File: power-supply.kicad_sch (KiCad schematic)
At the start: 9 parts, among them J1 KRE, J10 KRE, J12 Conn_01x04, J15 Conn_01x04, J3 KRE

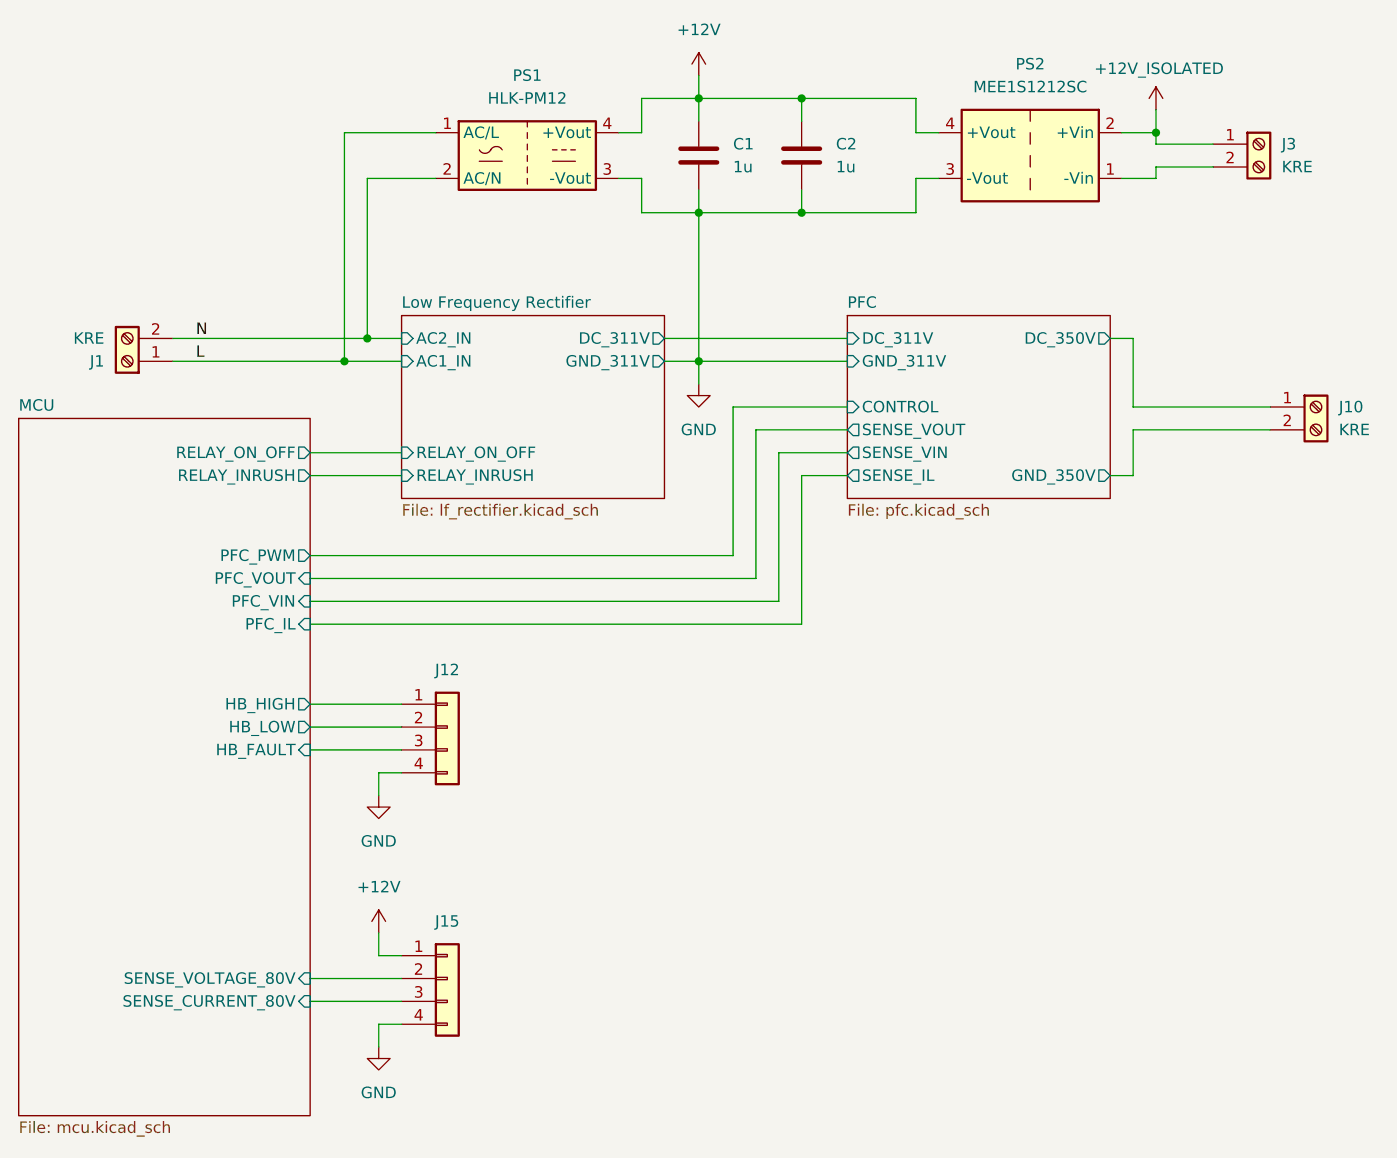
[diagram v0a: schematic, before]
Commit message: docs: add 3D renders, comprehensive README, CERN-OHL-S license, and update PCB routing
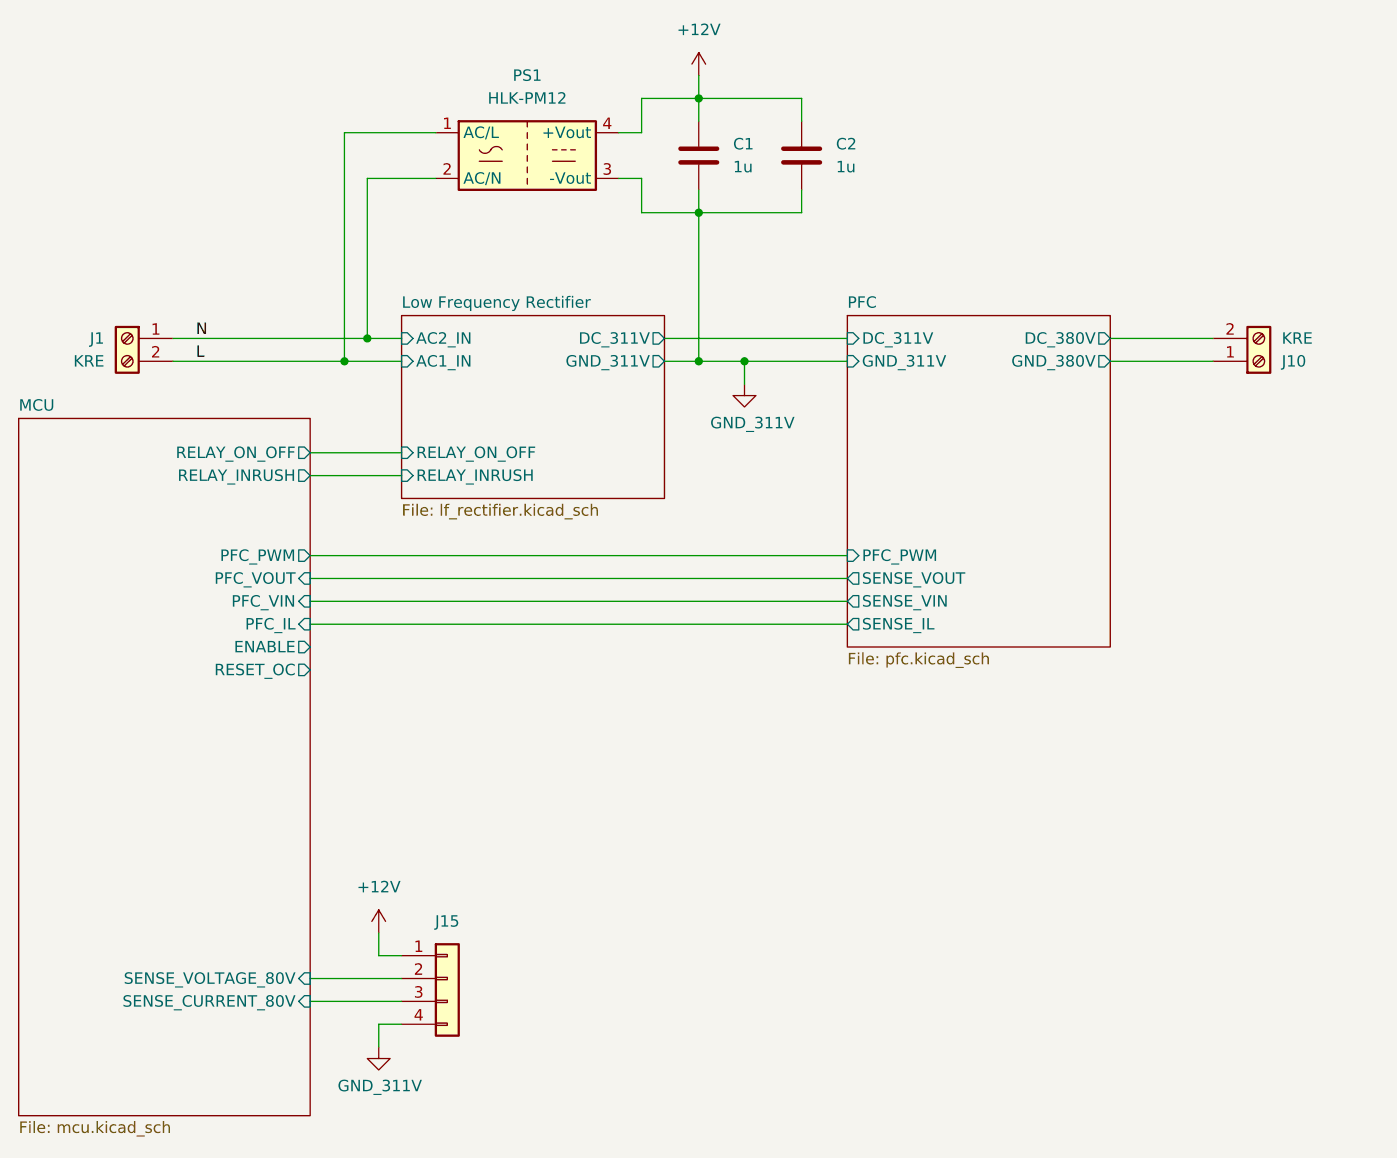
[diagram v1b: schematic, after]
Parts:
- removed J12: Conn_01x04, Connector_JST:JST_XH_B4B-XH-A_1x04_P2.50mm_Vertical, symbol Connector_Generic:Conn_01x04
- removed J3: KRE, TerminalBlock_Phoenix:TerminalBlock_Phoenix_MKDS-1,5-2-5.08_1x02_P5.08mm_Horizontal, symbol Connector:Screw_Terminal_01x02
- removed PS2: MEE1S1212SC, Converter_DCDC:Converter_DCDC_Murata_MEE1SxxxxSC_THT, symbol Converter_DCDC:MEE1S1212SC
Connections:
- net L: now also J1.2 (Pin_2); no longer J1.1 (Pin_1)
- net N: now also J1.1 (Pin_1); no longer J1.2 (Pin_2)
- net GND renamed GND_311V
- net PFC/DC_350V renamed PFC/GND_380V
- net PFC/GND_350V renamed PFC/DC_380V
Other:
- sheet MCU ports: added ENABLE, RESET_OC; removed HB_FAULT, HB_HIGH, HB_LOW
- sheet PFC ports: added DC_380V, GND_380V, PFC_PWM; removed CONTROL, DC_350V, GND_350V

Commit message: pcb: atualizar layout 2D da placa e esquematicos
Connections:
- net L: now also J1.1 (Pin_1); no longer J1.2 (Pin_2)
- net N: now also J1.2 (Pin_2); no longer J1.1 (Pin_1)
- net PFC/DC_380V: now also J10.1 (Pin_1); no longer J10.2 (Pin_2)
- net PFC/GND_380V: now also J10.2 (Pin_2); no longer J10.1 (Pin_1)
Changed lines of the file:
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@@
+	)
+	(symbol
+		(lib_id "Connector:Screw_Terminal_01x02")
+		(at 83.82 72.39 180)
+		(unit 1)
+		(body_style 1)
+		(exclude_from_sim no)
+		(in_bom yes)
+		(on_board yes)
+		(in_pos_files yes)
+		(dnp no)
+		(property "Reference" "J1"
+			(at 81.28 72.3901 0)
+			(show_name no)
+			(do_not_autoplace no)
+			(effects
+				(font
+					(size 1.27 1.27)
+				)
+				(justify left)
+			)
+		)
+		(property "Value" "KRE"
+			(at 81.28 69.8501 0)
+			(show_name no)
+			(do_not_autoplace no)
+			(effects
+				(font
+					(size 1.27 1.27)
+				)
+				(justify left)
+			)
+		)
+		(property "Footprint" "TerminalBlock_Phoenix:TerminalBlock_Phoenix_MKDS-1,5-2-5.08_1x02_P5.08mm_Horizontal"
+			(at 83.82 72.39 0)
+			(hide yes)
+			(show_name no)
+			(do_not_autoplace no)
+			(effects
+				(font
+					(size 1.27 1.27)
+				)
+			)
+		)
+		(property "Datasheet" ""
+			(at 83.82 72.39 0)
+			(hide yes)
+			(show_name no)
+			(do_not_autoplace no)
+			(effects
+				(font
+					(size 1.27 1.27)
+				)
+			)
+		)
+		(property "Description" "Generic screw terminal, single row, 01x02, script generated (kicad-library-utils/schlib/autogen/connector/)"
+			(at 83.82 72.39 0)
+			(hide yes)
+			(show_name no)
+			(do_not_autoplace no)
+			(effects
+				(font
+					(size 1.27 1.27)
+				)
+			)
+		)
+		(pin "1"
+		)
+		(pin "2"
+		)
+		(instances
+			(project "power-supply"
+				(path "/7202e823-25ba-4b77-8a88-a38eb2bf69b9"
+					(reference "J1")
+					(unit 1)
+				)
+			)
+		)
+	)
+	(symbol
+		(lib_id "Connector:Screw_Terminal_01x02")
+		(at 209.55 69.85 0)
+		(unit 1)
+		(body_style 1)
+		(exclude_from_sim no)
+		(in_bom yes)
+		(on_board yes)
+		(in_pos_files yes)
+		(dnp no)
+		(property "Reference" "J10"
+			(at 212.09 69.8499 0)
+			(show_name no)
+			(do_not_autoplace no)
+			(effects
+				(font
+					(size 1.27 1.27)
+				)
+				(justify left)
+			)
+		)
+		(property "Value" "KRE"
+			(at 212.09 72.3899 0)
+			(show_name no)
+			(do_not_autoplace no)
+			(effects
+				(font
+					(size 1.27 1.27)
+				)
+				(justify left)
+			)
+		)
+		(property "Footprint" "TerminalBlock_Phoenix:TerminalBlock_Phoenix_MKDS-1,5-2-5.08_1x02_P5.08mm_Horizontal"
+			(at 209.55 69.85 0)
+			(hide yes)
+			(show_name no)
+			(do_not_autoplace no)
+			(effects
+				(font
+					(size 1.27 1.27)
+				)
+			)
+		)
+		(property "Datasheet" ""
+			(at 209.55 69.85 0)
+			(hide yes)
+			(show_name no)
+			(do_not_autoplace no)
+			(effects
+				(font
+					(size 1.27 1.27)
+				)
+			)
+		)
+		(property "Description" "Generic screw terminal, single row, 01x02, script generated (kicad-library-utils/schlib/autogen/connector/)"
+			(at 209.55 69.85 0)
+			(hide yes)
+			(show_name no)
+			(do_not_autoplace no)
+			(effects
+				(font
+					(size 1.27 1.27)
+				)
+			)
+		)
+		(pin "1"
+		)
+		(pin "2"
+		)
+		(instances
+			(project "power-supply"
+				(path "/7202e823-25ba-4b77-8a88-a38eb2bf69b9"
+					(reference "J10")
+					(unit 1)
+				)
+			)
+		)
 	)
 	(symbol
@@
 	)
 	(symbol
-		(lib_id "Connector:Screw_Terminal_01x02")
-		(at 209.55 72.39 0)
-		(mirror x)
-		(unit 1)
-		(body_style 1)
-		(exclude_from_sim no)
-		(in_bom yes)
-		(on_board yes)
-		(in_pos_files yes)
-		(dnp no)
-		(property "Reference" "J10"
-			(at 212.09 72.3901 0)
-			(show_name no)
-			(do_not_autoplace no)
-			(effects
-				(font
-					(size 1.27 1.27)
-				)
-				(justify left)
-			)
-		)
-		(property "Value" "KRE"
-			(at 212.09 69.8501 0)
-			(show_name no)
-			(do_not_autoplace no)
-			(effects
-				(font
-					(size 1.27 1.27)
-				)
-				(justify left)
-			)
-		)
-		(property "Footprint" "TerminalBlock_Phoenix:TerminalBlock_Phoenix_MKDS-1,5-2-5.08_1x02_P5.08mm_Horizontal"
-			(at 209.55 72.39 0)
-			(hide yes)
-			(show_name no)
-			(do_not_autoplace no)
-			(effects
-				(font
-					(size 1.27 1.27)
-				)
-			)
-		)
-		(property "Datasheet" ""
-			(at 209.55 72.39 0)
-			(hide yes)
-			(show_name no)
-			(do_not_autoplace no)
-			(effects
-				(font
-					(size 1.27 1.27)
-				)
-			)
-		)
-		(property "Description" "Generic screw terminal, single row, 01x02, script generated (kicad-library-utils/schlib/autogen/connector/)"
-			(at 209.55 72.39 0)
-			(hide yes)
-			(show_name no)
-			(do_not_autoplace no)
-			(effects
-				(font
-					(size 1.27 1.27)
-				)
-			)
-		)
-		(pin "1"
-		)
-		(pin "2"
-		)
-		(instances
-			(project "power-supply"
-				(path "/7202e823-25ba-4b77-8a88-a38eb2bf69b9"
-					(reference "J10")
-					(unit 1)
-				)
-			)
-		)
-	)
-	(symbol
 		(lib_id "power:+12V")
 		(at 147.32 40.64 0)
@@
 					(unit 1)
 				)
-			)
-		)
-	)
-	(symbol
-		(lib_id "Connector:Screw_Terminal_01x02")
-		(at 83.82 69.85 0)
-		(mirror y)
-		(unit 1)
-		(body_style 1)
-		(exclude_from_sim no)
-		(in_bom yes)
-		(on_board yes)
-		(in_pos_files yes)
-		(dnp no)
-		(property "Reference" "J1"
-			(at 81.28 69.8499 0)
-			(show_name no)
-			(do_not_autoplace no)
-			(effects
-				(font
-					(size 1.27 1.27)
-				)
-				(justify left)
-			)
-		)
-		(property "Value" "KRE"
-			(at 81.28 72.3899 0)
-			(show_name no)
-			(do_not_autoplace no)
-			(effects
-				(font
-					(size 1.27 1.27)
-				)
-				(justify left)
-			)
-		)
-		(property "Footprint" "TerminalBlock_Phoenix:TerminalBlock_Phoenix_MKDS-1,5-2-5.08_1x02_P5.08mm_Horizontal"
-			(at 83.82 69.85 0)
-			(hide yes)
-			(show_name no)
-			(do_not_autoplace no)
-			(effects
-				(font
-					(size 1.27 1.27)
-				)
-			)
-		)
-		(property "Datasheet" ""
-			(at 83.82 69.85 0)
-			(hide yes)
-			(show_name no)
-			(do_not_autoplace no)
-			(effects
-				(font
-					(size 1.27 1.27)
-				)
-			)
-		)
-		(property "Description" "Generic screw terminal, single row, 01x02, script generated (kicad-library-utils/schlib/autogen/connector/)"
-			(at 83.82 69.85 0)
-			(hide yes)
-			(show_name no)
-			(do_not_autoplace no)
-			(effects
-				(font
-					(size 1.27 1.27)
-				)
-			)
-		)
-		(pin "1"
-		)
-		(pin "2"
-		)
-		(instances
-			(project "power-supply"
-				(path "/7202e823-25ba-4b77-8a88-a38eb2bf69b9"
-					(reference "J1")
-					(unit 1)
-				)
